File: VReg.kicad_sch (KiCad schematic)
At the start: 17 parts

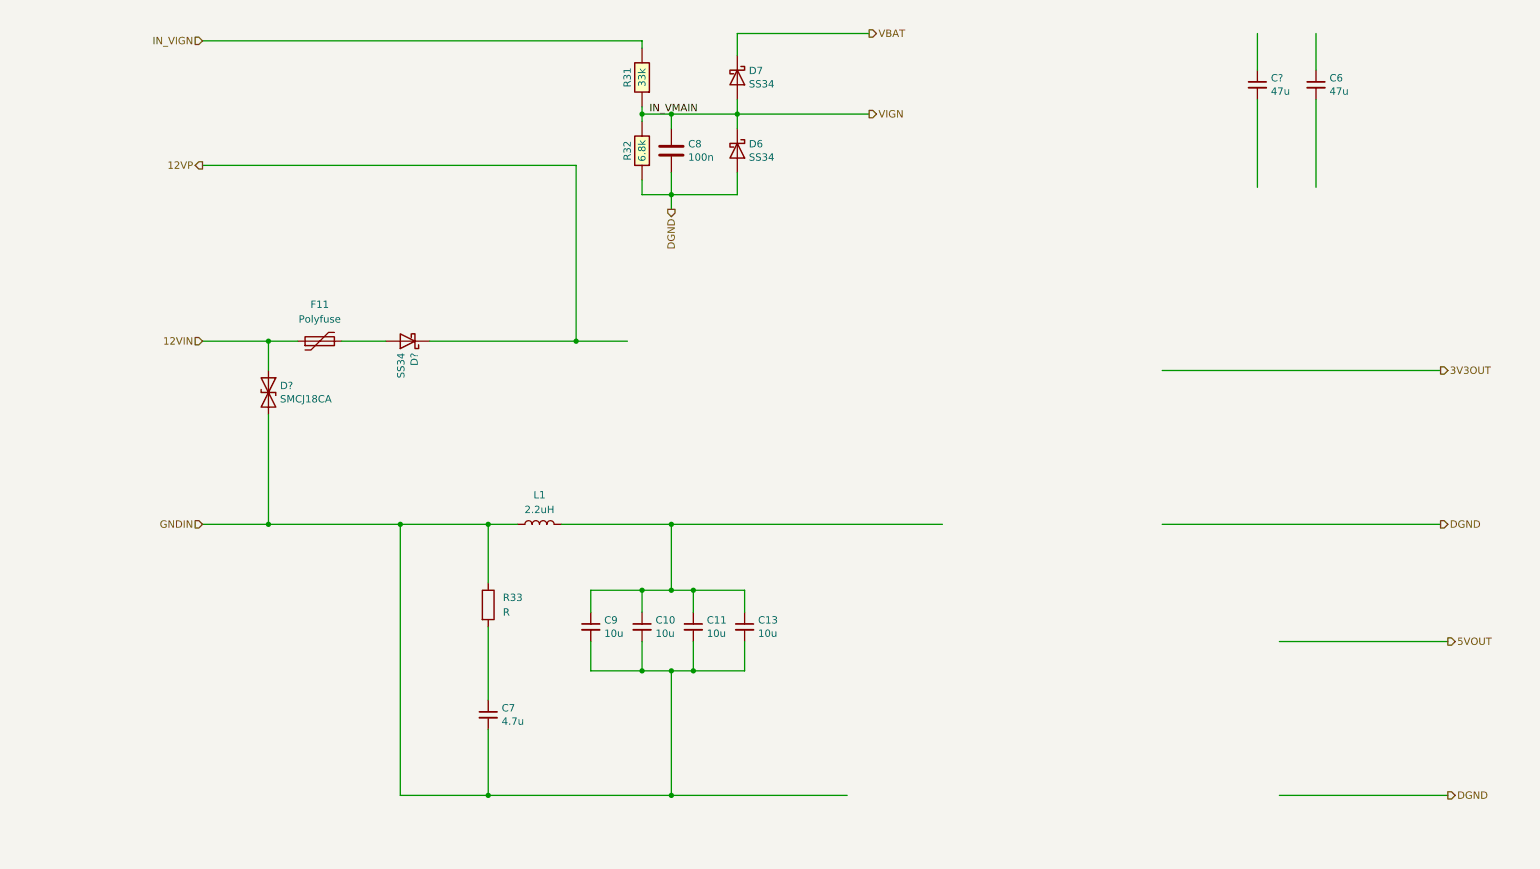
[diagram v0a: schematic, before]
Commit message: Standalone version without hellen-one
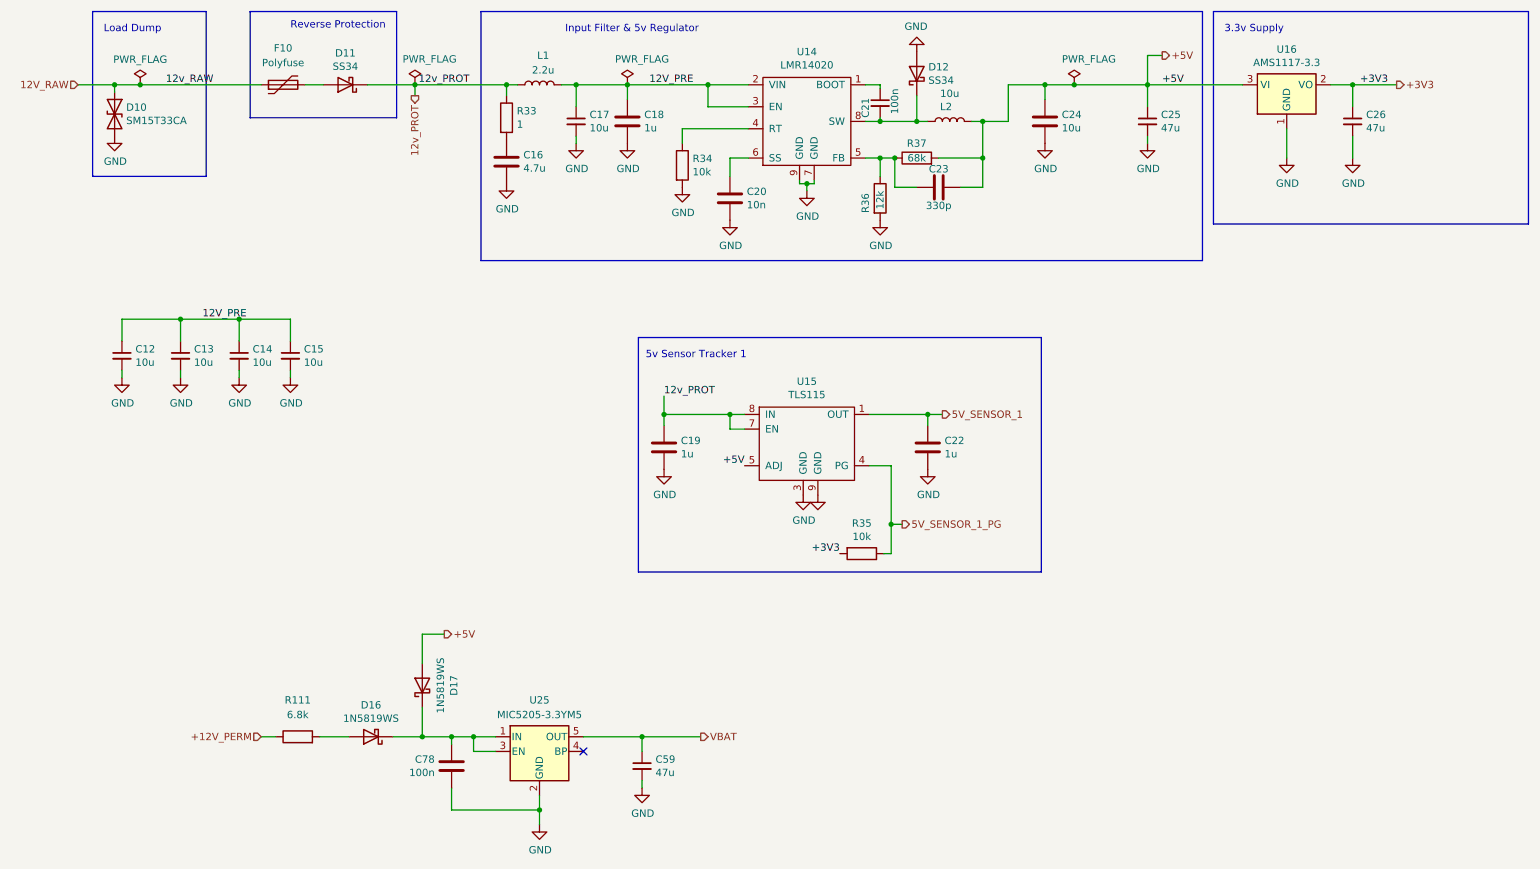
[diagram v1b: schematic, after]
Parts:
- removed C10, C11, C9: 10u, Capacitor_SMD:C_1206_3216Metric, symbol Device:C_Small
- removed C6, C?: 47u, Capacitor_SMD:C_1206_3216Metric, symbol Device:C_Small
- removed C7: 4.7u, Capacitor_SMD:C_0603_1608Metric, symbol Device:C_Small
- removed C8: 100n, Capacitor_SMD:C_0402_1005Metric, symbol Device:C
- removed D6, D7, D?: SS34, Diode_SMD:D_SMA, symbol Device:D_Schottky
- removed D?: SMCJ18CA, Diode_SMD:D_SMC, symbol Device:D_TVS
- removed R31: 33k, hellen-one-common:R0603, symbol hellen-one-common:Res
- removed R32: 6.8k, hellen-one-common:R0603, symbol hellen-one-common:Res
- added C12, C14, C15, C17: 10u, Capacitor_SMD:C_0805_2012Metric, symbol Device:C_Small
- added C16: 4.7u, Capacitor_SMD:C_0603_1608Metric, symbol Device:C
- added C18, C19, C22: 1u, Capacitor_SMD:C_0603_1608Metric, symbol Device:C
- added C20: 10n, Capacitor_SMD:C_0603_1608Metric, symbol Device:C
- added C21: 100n, Capacitor_SMD:C_0402_1005Metric, symbol Device:C_Small
- added C23: 330p, Capacitor_SMD:C_0402_1005Metric, symbol Device:C
- added C24: 10u, Capacitor_SMD:C_1206_3216Metric, symbol Device:C
- added C25, C26, C59: 47u, Capacitor_SMD:C_1206_3216Metric, symbol Device:C_Small
- added C78: 100n, Capacitor_SMD:C_0402_1005Metric, symbol Device:C
- added D10: SM15T33CA, Diode_SMD:D_SMC, symbol Device:D_TVS
- added D11, D12: SS34, Diode_SMD:D_SMA, symbol Device:D_Schottky
- added D16, D17: 1N5819WS, Diode_SMD:D_SOD-123, symbol Device:D_Schottky
- added L2: 10u, sunlord-MWSA0503:MWSA0503, symbol Device:L
- added R111: 6.8k, Resistor_SMD:R_0603_1608Metric, symbol Device:R
- added R34, R35: 10k, Resistor_SMD:R_0402_1005Metric, symbol Device:R
- added R36: 12k, Resistor_SMD:R_0402_1005Metric, symbol Device:R
- added R37: 68k, Resistor_SMD:R_0402_1005Metric, symbol Device:R
- added U14: LMR14020, Package_SO:SOIC-8-1EP_3.9x4.9mm_P1.27mm_EP2.29x3mm, symbol lmr14020:LMR14020
- added U15: TLS115, Package_SO:Infineon_PG-DSO-8-43, symbol infineon_psu:TLS115
- added U16: AMS1117-3.3, Package_TO_SOT_SMD:SOT-223-3_TabPin2, symbol Regulator_Linear:AMS1117-3.3
- added U25: MIC5205-3.3YM5, Package_TO_SOT_SMD:SOT-23-5, symbol Regulator_Linear:MIC5205-3.3YM5
- C13: footprint Capacitor_SMD:C_1206_3216Metric -> Capacitor_SMD:C_0805_2012Metric; LCSC C13585 -> C440198; Vrat (none) -> 50V
- L1: value 2.2uH -> 2.2u; LCSC C36828 -> C75646; LCSC_ext (none) -> 1; PN (none) -> SRN3015TA-2R2M; possible_not_ext (none) -> 1
- R33: value R -> 1; footprint Resistor_SMD:R_0603_1608Metric -> Resistor_SMD:R_0402_1005Metric; LCSC C22936 -> C25086; LCSC_ext (none) -> 0
- renumbered F11 to F10
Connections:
- net VBAT: now also C59.1, U25.5 (OUT)
- net at F10.2: now also D11.2 (A)
- net 12V_PRE: now reaches C13.1, L1.2
- net 12V_PRE: now also C12.1, C14.1, C15.1, C17.1, C18.1, U14.2 (VIN), U14.3 (EN)
- net at R33.2: now also C16.1
- net 12VIN renamed 12V_RAW
- net 12V_RAW: now also D10.1 (A1)
- net GNDIN renamed 12v_PROT
- net 12v_PROT: now also C19.1, D11.1 (K), U15.7 (EN), U15.8 (IN); no longer C13.2
- new net: C21.2, D12.1 (K), L2.1, U14.8 (SW)
- new net: C21.1, U14.1 (BOOT)
- new net: R34.1, U14.4 (RT)
- new net: C23.2, R36.1, R37.1, U14.5 (FB)
- new net: C20.1, U14.6 (SS)
- new net: C78.1, D16.1 (K), D17.1 (K), U25.1 (IN), U25.3 (EN)
- new net: D16.2 (A), R111.2
- new net +12V_PERM: R111.1
- new net +3V3: C26.1, R35.2, U16.2 (VO)
- new net +5V: C23.1, C24.1, C25.1, D17.2 (A), L2.2, R37.2, U15.5 (ADJ), U16.3 (VI)
- new net 5V_SENSOR_1: C22.1, U15.1 (OUT)
- new net 5V_SENSOR_1_PG: R35.1, U15.4 (PG)
- new net GND: C12.2, C13.2, C14.2, C15.2, C16.2, C17.2, C18.2, C19.2, C20.2, C22.2, C24.2, C25.2, C26.2, C59.2, C78.2, D10.2 (A2), D12.2 (A), R34.2, R36.2, U14.7 (GND), U14.9 (GND), U15.3 (GND), U15.9 (GND), U16.1 (GND), U25.2 (GND)
- no-connect marks 0 -> 1
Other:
- note added: "3.3v Supply"
- note added: "5v Sensor Tracker 1"
- note added: "Input Filter & 5v Regulator"
- note added: "Load Dump"
- note added: "Reverse Protection"
- moved on the sheet: F10
